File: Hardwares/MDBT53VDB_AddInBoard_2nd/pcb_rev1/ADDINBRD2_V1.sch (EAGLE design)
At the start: 0 parts

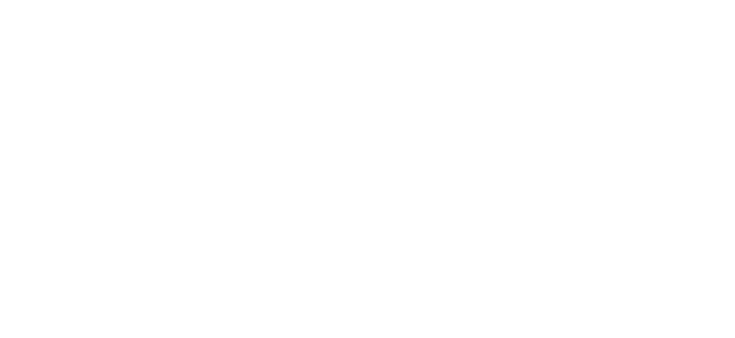
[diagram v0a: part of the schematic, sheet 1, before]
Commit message: 回路図を修正
・表題を追加
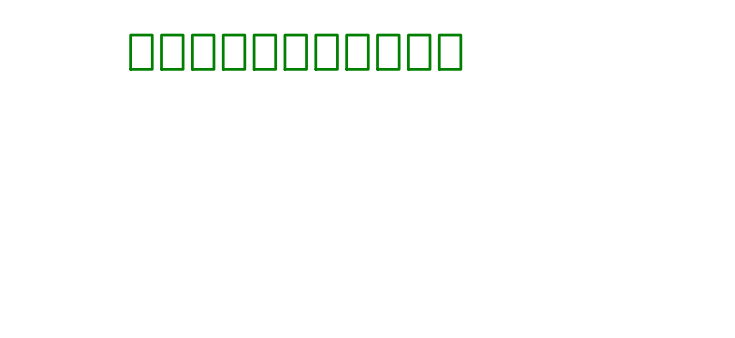
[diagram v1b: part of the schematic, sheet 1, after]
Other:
- note added: "動作電源投入・遮断回路"
- note added: "電源電圧測定回路"
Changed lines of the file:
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@@
 <text x="167.64" y="8.89" size="3.81" layer="91">Add-in board 2nd
 for MDBT53V-DB</text>
+<text x="129.54" y="152.4" size="3.81" layer="91" align="bottom-center">動作電源投入・遮断回路</text>
 </plain>
 <instances>
@@
 <text x="167.64" y="8.89" size="3.81" layer="91">Add-in board 2nd
 for MDBT53V-DB</text>
+<text x="129.54" y="152.4" size="3.81" layer="91" align="bottom-center">電源電圧測定回路</text>
 </plain>
 <instances>

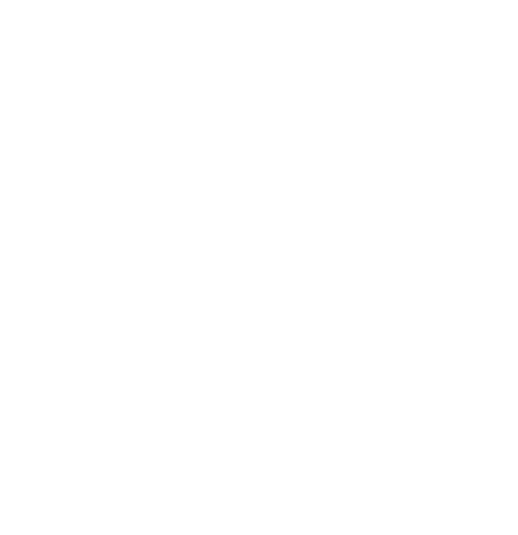
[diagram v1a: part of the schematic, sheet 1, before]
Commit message: レイアウトを修正
・リセッタブルヒューズを配置
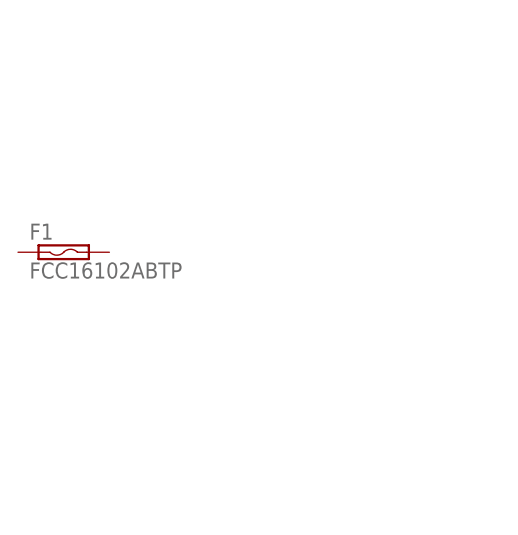
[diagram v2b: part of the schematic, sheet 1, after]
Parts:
- added F1: FCC16102ABTP, Parts:FCC16102ABTP
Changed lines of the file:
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@@
 <part name="FRAME1" library="Generic" deviceset="A4L-LOC" device=""/>
 <part name="FRAME2" library="Generic" deviceset="A4L-LOC" device=""/>
+<part name="F1" library="Parts" deviceset="FCC16" device="102ABTP"/>
 </parts>
 <sheets>
@@
 <instances>
 <instance part="FRAME1" gate="G$1" x="0" y="0"/>
+<instance part="F1" gate="G$1" x="53.34" y="132.08"/>
 </instances>
 <busses>

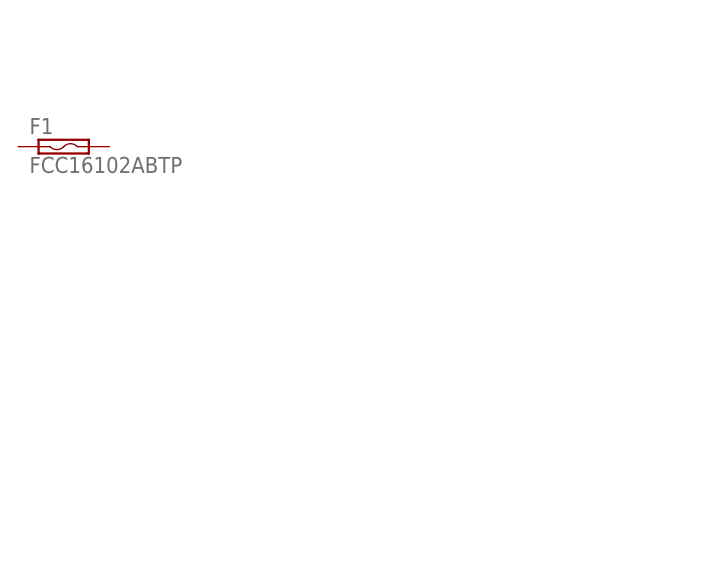
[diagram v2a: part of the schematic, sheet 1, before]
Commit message: レイアウトを修正
・SBD（極性逆転阻止用）を配置
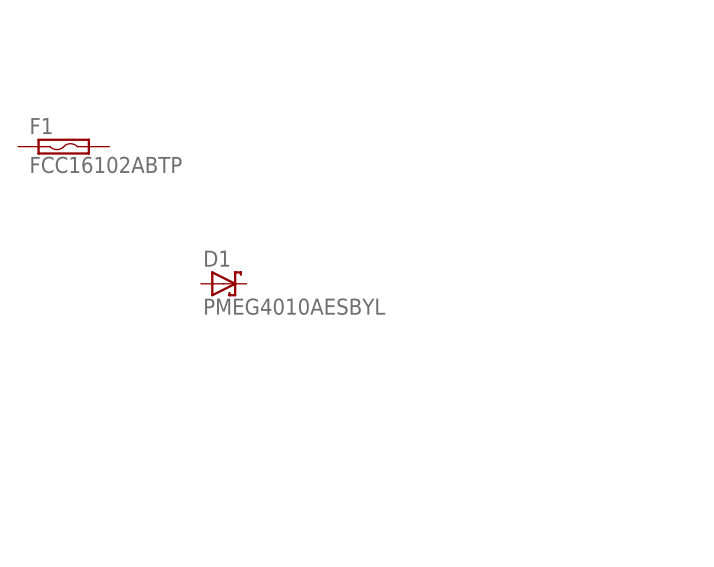
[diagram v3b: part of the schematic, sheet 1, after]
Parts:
- added D1: PMEG4010AESBYL, Parts:PMEG4010AESBYL
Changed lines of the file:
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@@
 <part name="FRAME2" library="Generic" deviceset="A4L-LOC" device=""/>
 <part name="F1" library="Parts" deviceset="FCC16" device="102ABTP"/>
+<part name="D1" library="Parts" deviceset="PMEG4010" device="AESBYL"/>
 </parts>
 <sheets>
@@
 <instance part="FRAME1" gate="G$1" x="0" y="0"/>
 <instance part="F1" gate="G$1" x="53.34" y="132.08"/>
+<instance part="D1" gate="G$1" x="71.12" y="116.84"/>
 </instances>
 <busses>

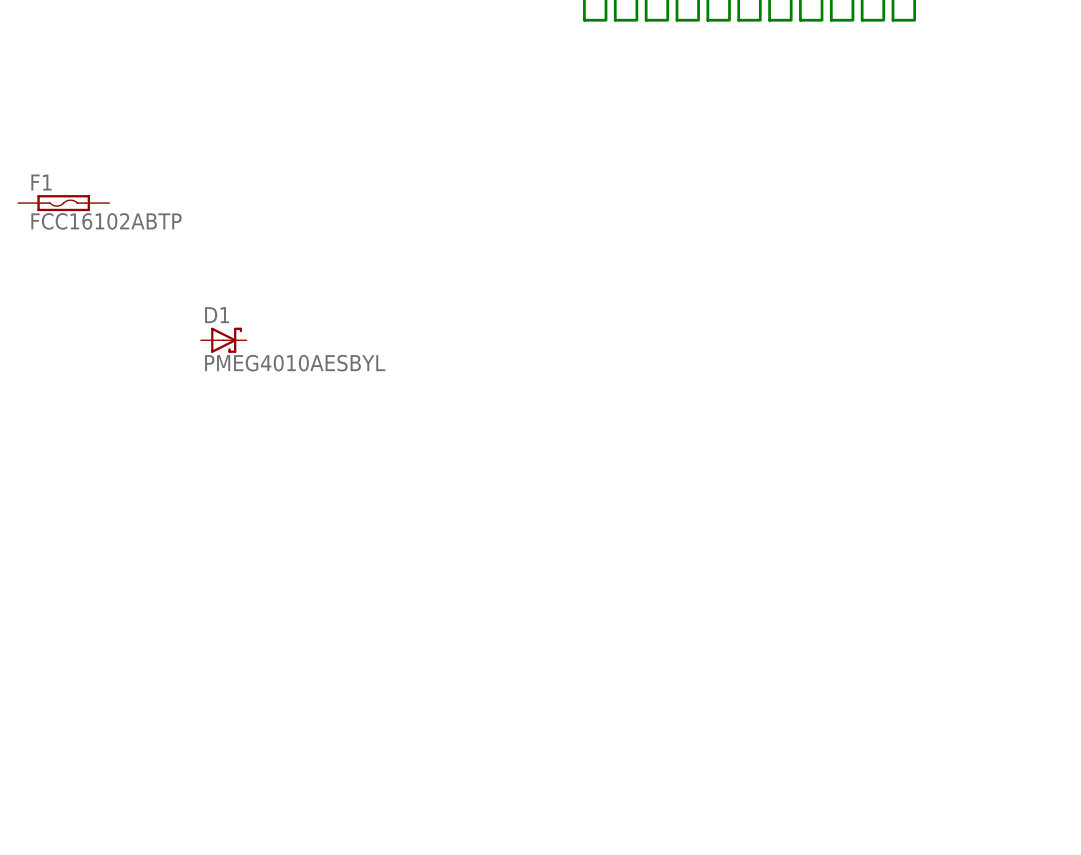
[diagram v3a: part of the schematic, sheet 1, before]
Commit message: レイアウトを修正
・汎用部品を配置
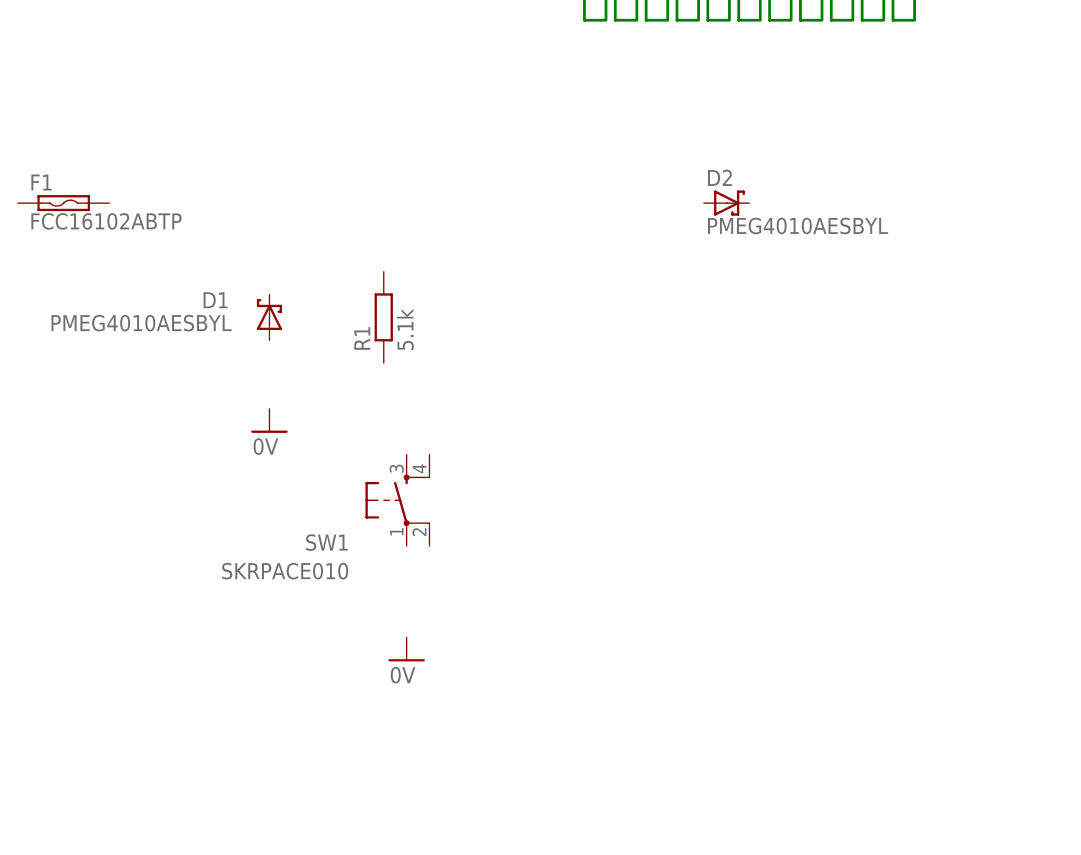
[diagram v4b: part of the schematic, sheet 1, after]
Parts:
- added D2: PMEG4010AESBYL, Parts:PMEG4010AESBYL
- added R1: 5.1k, Parts:RESISTOR_0402N
- added SW1: SKRPACE010, Parts:SKRPACE010
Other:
- moved on the sheet: D1
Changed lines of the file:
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@@
 <part name="F1" library="Parts" deviceset="FCC16" device="102ABTP"/>
 <part name="D1" library="Parts" deviceset="PMEG4010" device="AESBYL"/>
+<part name="SW1" library="Parts" deviceset="SKRPACE010" device=""/>
+<part name="GND1" library="Supply" deviceset="0V" device=""/>
+<part name="GND2" library="Supply" deviceset="0V" device=""/>
+<part name="R1" library="Parts" deviceset="RESISTOR" device="_0402N" value="5.1k"/>
+<part name="D2" library="Parts" deviceset="PMEG4010" device="AESBYL"/>
 </parts>
 <sheets>
@@
 <instance part="FRAME1" gate="G$1" x="0" y="0"/>
 <instance part="F1" gate="G$1" x="53.34" y="132.08"/>
-<instance part="D1" gate="G$1" x="71.12" y="116.84"/>
+<instance part="D1" gate="G$1" x="76.2" y="119.38" smashed="yes" rot="R90">
+<attribute name="NAME" x="71.755" y="122.174" size="1.778" layer="95" rot="R180"/>
+<attribute name="VALUE" x="72.009" y="119.634" size="1.778" layer="96" rot="R180"/>
+</instance>
+<instance part="SW1" gate="G$1" x="91.44" y="99.06" smashed="yes">
+<attribute name="NAME" x="85.09" y="95.25" size="1.778" layer="95" rot="R180"/>
+<attribute name="VALUE" x="85.09" y="92.075" size="1.778" layer="96" rot="R180"/>
+</instance>
+<instance part="GND1" gate="1" x="76.2" y="106.68"/>
+<instance part="GND2" gate="1" x="91.44" y="81.28"/>
+<instance part="R1" gate="G$1" x="88.9" y="114.3" rot="R90"/>
+<instance part="D2" gate="G$1" x="127" y="132.08"/>
 </instances>
 <busses>

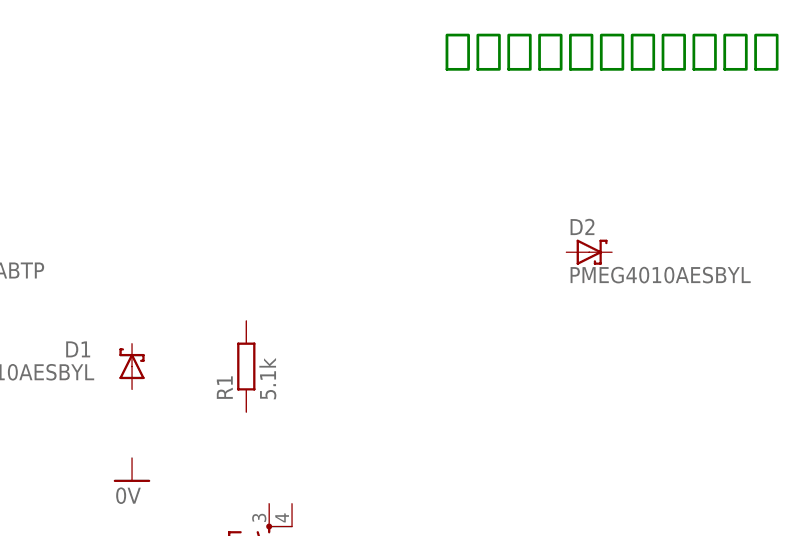
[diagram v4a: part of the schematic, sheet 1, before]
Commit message: レイアウトを修正
・MOSFETを配置
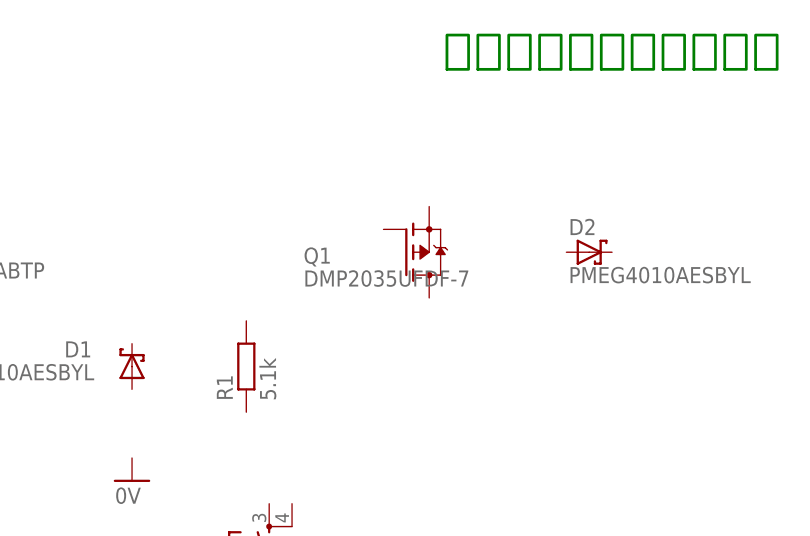
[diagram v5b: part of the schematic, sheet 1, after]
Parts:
- added Q1: DMP2035UFDF-7, Parts:DMP2035UFDF-7
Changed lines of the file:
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@@
 <part name="R1" library="Parts" deviceset="RESISTOR" device="_0402N" value="5.1k"/>
 <part name="D2" library="Parts" deviceset="PMEG4010" device="AESBYL"/>
+<part name="Q1" library="Parts" deviceset="DMP2035" device="UFDF-7"/>
 </parts>
 <sheets>
@@
 <instance part="R1" gate="G$1" x="88.9" y="114.3" rot="R90"/>
 <instance part="D2" gate="G$1" x="127" y="132.08"/>
+<instance part="Q1" gate="G$1" x="106.68" y="132.08"/>
 </instances>
 <busses>

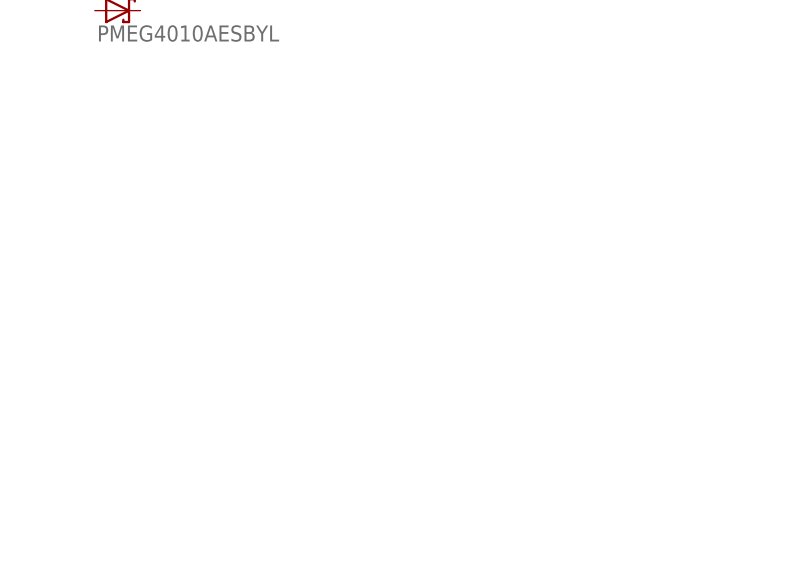
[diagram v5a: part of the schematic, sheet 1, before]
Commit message: レイアウトを修正
・ロジックICを配置
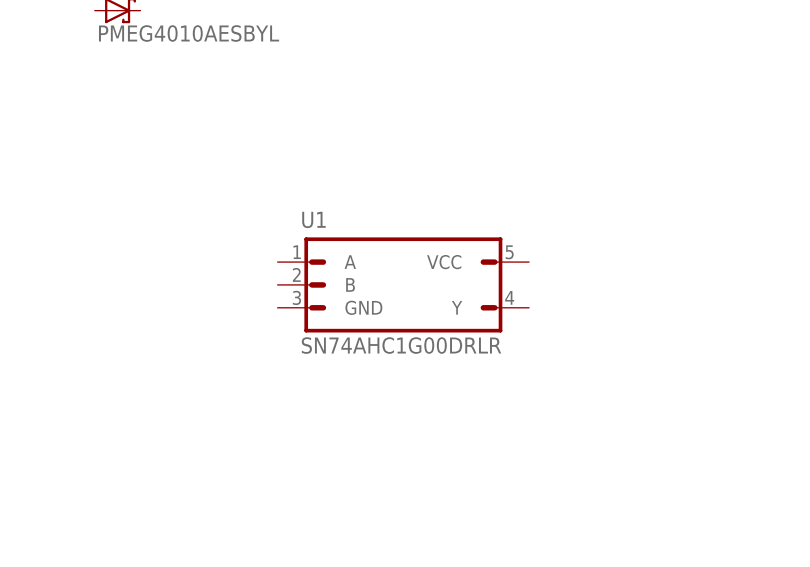
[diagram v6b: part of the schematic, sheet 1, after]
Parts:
- added U1: SN74AHC1G00DRLR, Parts:SN74AHC1G00DRLR
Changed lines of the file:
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@@
 <part name="D2" library="Parts" deviceset="PMEG4010" device="AESBYL"/>
 <part name="Q1" library="Parts" deviceset="DMP2035" device="UFDF-7"/>
+<part name="U1" library="Parts" deviceset="SN74AHC1G00" device="DRLR"/>
 </parts>
 <sheets>
@@
 <instance part="D2" gate="G$1" x="127" y="132.08"/>
 <instance part="Q1" gate="G$1" x="106.68" y="132.08"/>
+<instance part="U1" gate="G$1" x="144.78" y="104.14"/>
 </instances>
 <busses>
